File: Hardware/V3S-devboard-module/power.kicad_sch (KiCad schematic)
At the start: 19 parts, among them U2 EA3036C

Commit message: schematic improvements
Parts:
- added C14, C15: 106, symbol Device:C_Small
- added C16, C17, C20, C23, C25, C26, C29, C30, C33, C34, C35, C36, C37, C38, C39, C43: 100n, symbol Device:C_Small
- added C18, C21, C27, C31, C42: 10u, symbol Device:C_Small
- added C19, C22, C24, C28, C32, C40: 1u, symbol Device:C_Small
- added C41, C44: 4.7u, symbol Device:C_Small
- added R1: 0, symbol Device:R_Small_US
- added R12, R13: 2K, symbol Device:R_Small_US
- added R14: 200K, symbol Device:R_Small_US
- added U3: XC6206PxxxMR, Package_TO_SOT_SMD:SOT-23-3, symbol Regulator_Linear:XC6206PxxxMR
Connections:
- net 1V2: now also C21.2, C24.2, C25.2, C26.2, C27.2, C28.2, C29.2, C30.2
- net 1V8: now also C18.2, C19.2, C20.2, C22.2, C23.2, R12.1
- net 3V3: now also C31.2, C32.2, C33.2, C34.2, C35.2, C36.2, C39.2, R1.2, U3.3 (VI)
- net GND: now also C14.1, C15.1, C16.1, C17.1, C18.1, C19.1, C20.1, C21.1, C22.1, C23.1, C24.1, C25.1, C26.1, C27.1, C28.1, C29.1, C30.1, C31.1, C32.1, C33.1, C34.1, C35.1, C36.1, C37.1, C38.1, C39.1, C40.1, C41.1, C42.1, C43.1, C44.1, R13.2, R14.2, U3.1 (GND)
- net SVREF: now also C16.2, C17.2, R12.2, R13.1
- net VCC_HP_BP: now also C42.2, C43.2
- net VCC_RTC: now also C37.2, R1.1
- net VCC_RTCIO: now also C44.2
- net VRA1: now also C40.2
- net VRA2: now also C41.2, R14.1
- new net 3V0: C14.2, C15.2, C38.2, U3.2 (VO)

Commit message: general improvements. power almost complete
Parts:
- added C46: 10u, Capacitor_SMD:C_0805_2012Metric, symbol Device:C_Small
- C1, C14, C15: value 106 -> 1u; footprint (none) -> Capacitor_SMD:C_0805_2012Metric
- C16, C17, C20, C23, C25, C26, C29, C30, C33, C34, C35, C36, C37, C38, C39, C4, C43, C5, C6: footprint (none) -> Capacitor_SMD:C_0603_1608Metric
- C18, C19, C21, C22, C24, C27, C28, C31, C32, C40, C41, C42, C44: footprint (none) -> Capacitor_SMD:C_0805_2012Metric
- C2, C3, C7, C8, C9: value 106 -> 10u; footprint (none) -> Capacitor_SMD:C_0805_2012Metric
- L1, L2, L3: footprint (none) -> Inductor_SMD:L_1008_2520Metric
- R12, R13, R14, R2, R3, R4, R5, R6, R7: footprint (none) -> Resistor_SMD:R_0603_1608Metric
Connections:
- net 3V0: no longer C15.2
- net 3V3: now also C15.2
- net 5V: now also C46.1
- net GND: now also C46.2
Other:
- note added: "1uF near VCC 10uF near VINx"
- note added: "DC resistance must be < 100 milliohms Current rating 1.1A"
- moved on the sheet: C1, C2, C3

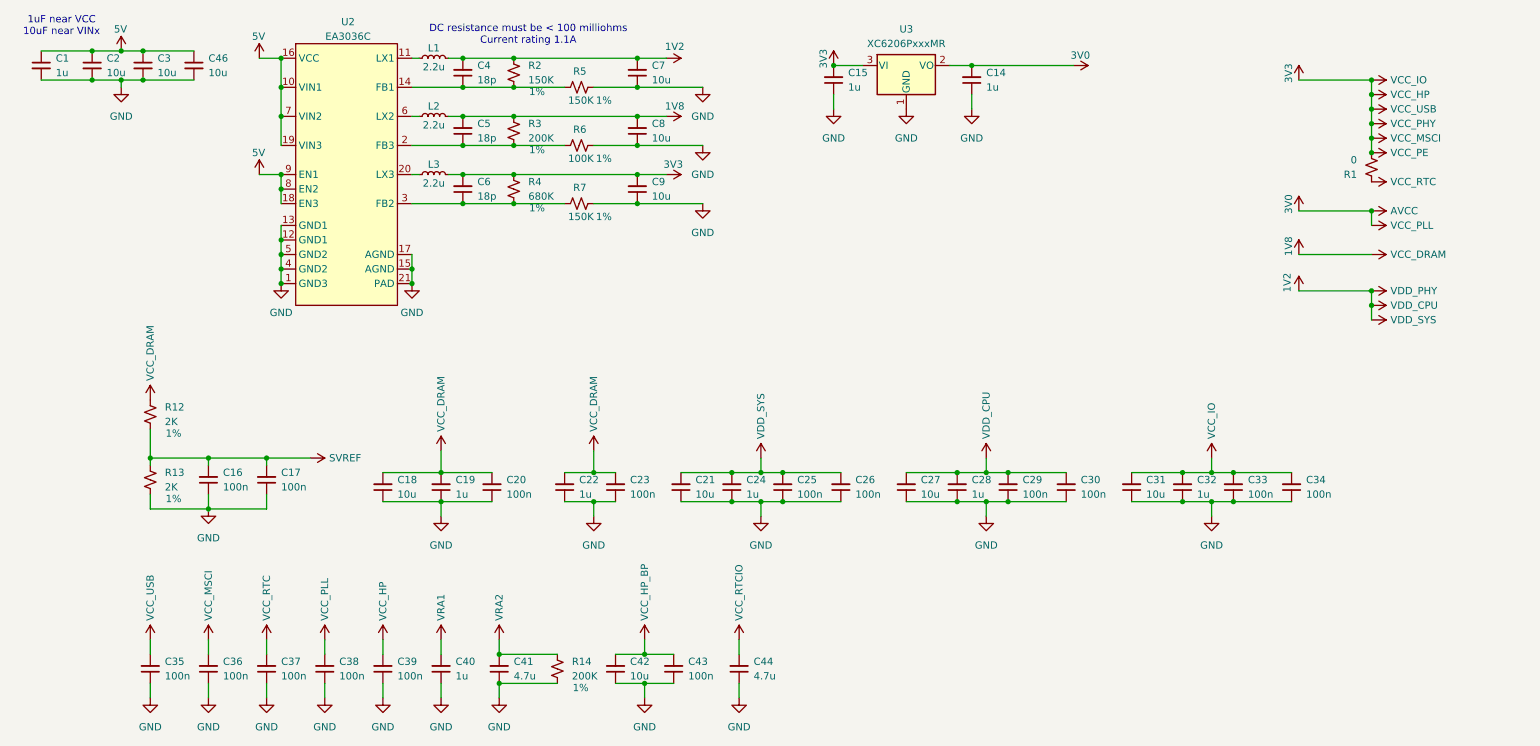
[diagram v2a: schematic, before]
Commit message: new power designators
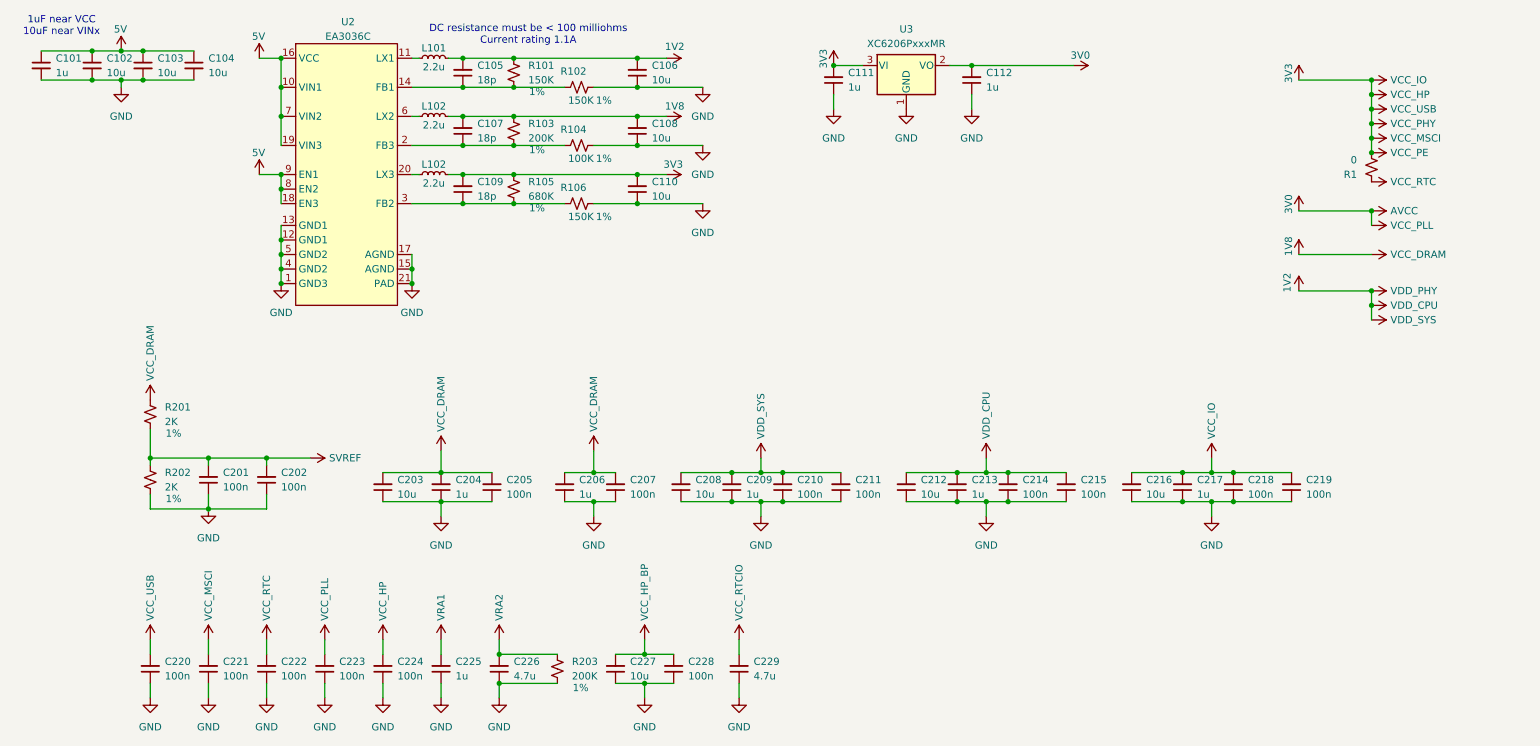
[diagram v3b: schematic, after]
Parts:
- renumbered C1 to C101, C2 to C102, C3 to C103, C46 to C104, C4 to C105, C7 to C106, C5 to C107, C8 to C108, C6 to C109, C9 to C110, C15 to C111, C14 to C112, C16 to C201, C17 to C202, C18 to C203, C19 to C204, C20 to C205, C22 to C206, C23 to C207, C21 to C208, C24 to C209, C25 to C210, C26 to C211, C27 to C212, C28 to C213, C29 to C214, C30 to C215, C31 to C216, C32 to C217, C33 to C218, C34 to C219, C35 to C220, C36 to C221, C37 to C222, C38 to C223, C39 to C224, C40 to C225, C41 to C226, C42 to C227, C43 to C228, C44 to C229, L1 to L101, L2 to L102, L3 to L102, R2 to R101, R5 to R102, R3 to R103, R6 to R104, R4 to R105, R7 to R106, R12 to R201, R13 to R202, R14 to R203

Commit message: minor improvements and fixes
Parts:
- R106: renamed from R1; footprint (none) -> Resistor_SMD:R_0603_1608Metric
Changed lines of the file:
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@@
 		(on_board yes)
 		(dnp no)
-		(property "Reference" "R1"
+		(property "Reference" "R106"
 			(at 255.27 58.4201 0)
 			(effects
@@
 			)
 		)
-		(property "Footprint" ""
+		(property "Footprint" "Resistor_SMD:R_0603_1608Metric"
 			(at 257.81 57.15 0)
 			(effects
@@
 			(project "V3S-devboard-module"
 				(path "/5d41c08e-2331-42df-a2d5-1aeb6ed4388c/5949d9b7-76b3-40a2-8931-5cd58c7934ef"
-					(reference "R1")
+					(reference "R106")
 					(unit 1)
 				)

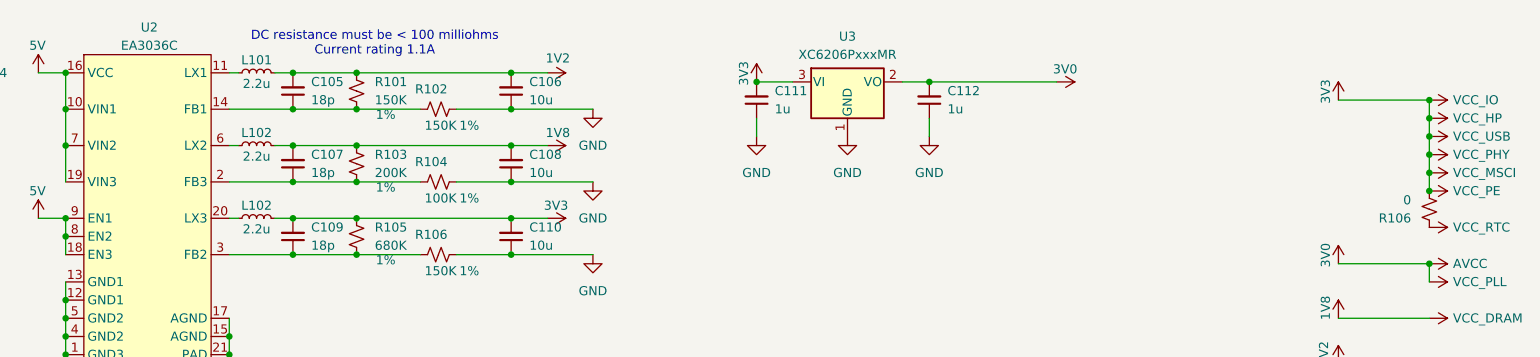
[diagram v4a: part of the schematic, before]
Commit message: fixed minor schematic issues
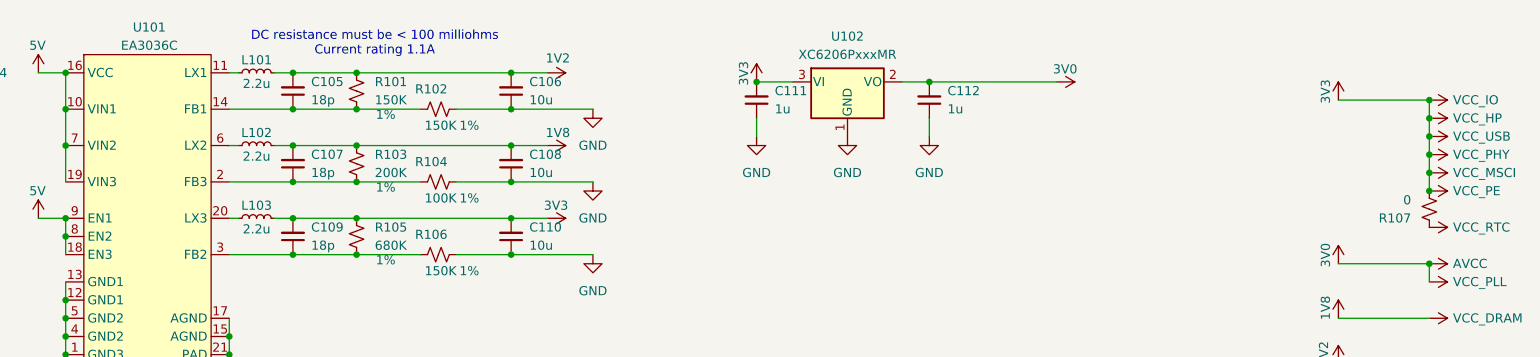
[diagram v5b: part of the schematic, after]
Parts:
- renumbered L102 to L103, R106 to R107, U2 to U101, U3 to U102
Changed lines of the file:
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@@
 		(dnp no)
 		(fields_autoplaced yes)
-		(property "Reference" "U3"
+		(property "Reference" "U102"
 			(at 176.53 33.02 0)
 			(effects
@@
 			(project "V3S-devboard-module"
 				(path "/5d41c08e-2331-42df-a2d5-1aeb6ed4388c/5949d9b7-76b3-40a2-8931-5cd58c7934ef"
-					(reference "U3")
+					(reference "U102")
 					(unit 1)
 				)
@@
 		(on_board yes)
 		(dnp no)
-		(property "Reference" "L102"
+		(property "Reference" "L103"
 			(at 93.98 56.642 90)
 			(effects
@@
 			(project "V3S-devboard-module"
 				(path "/5d41c08e-2331-42df-a2d5-1aeb6ed4388c/5949d9b7-76b3-40a2-8931-5cd58c7934ef"
-					(reference "L102")
+					(reference "L103")
 					(unit 1)
 				)
@@
 		(on_board yes)
 		(dnp no)
-		(property "Reference" "R106"
+		(property "Reference" "R107"
 			(at 255.27 58.4201 0)
 			(effects
@@
 			(project "V3S-devboard-module"
 				(path "/5d41c08e-2331-42df-a2d5-1aeb6ed4388c/5949d9b7-76b3-40a2-8931-5cd58c7934ef"
-					(reference "R106")
+					(reference "R107")
 					(unit 1)
 				)
@@
 		(on_board yes)
 		(dnp no)
-		(property "Reference" "U2"
+		(property "Reference" "U101"
 			(at 78.994 31.75 0)
 			(effects
@@
 			(project "V3S-devboard-module"
 				(path "/5d41c08e-2331-42df-a2d5-1aeb6ed4388c/5949d9b7-76b3-40a2-8931-5cd58c7934ef"
-					(reference "U2")
+					(reference "U101")
 					(unit 1)
 				)

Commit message: layout improvements.
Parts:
- added NT1: NetTie_2, NetTie:NetTie-2_SMD_Pad2.0mm, symbol Device:NetTie_2
- C101, C102, C103, C104, C106, C108, C110, C111, C112, C203, C204, C206, C208, C209, C212, C213, C216, C217, C225, C226, C227, C229: footprint Capacitor_SMD:C_0805_2012Metric -> Capacitor_SMD:C_0603_1608Metric
- C105, C107, C109, C202, C205, C207, C210, C211, C214, C215, C218, C219, C220, C221, C222, C223, C224, C228: footprint Capacitor_SMD:C_0603_1608Metric -> Capacitor_SMD:C_0402_1005Metric
- R101, R102, R103, R104, R105, R106, R201, R202, R203: footprint Resistor_SMD:R_0603_1608Metric -> Resistor_SMD:R_0402_1005Metric
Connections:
- net 1V8: now also NT1.1; no longer C203.2, C204.2, C205.2, C206.2, C207.2, R201.1
- new net VCC_DRAM: C203.2, C204.2, C205.2, C206.2, C207.2, NT1.2, R201.1
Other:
- moved on the sheet: C206, C207

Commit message: some layout
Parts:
- removed NT1: NetTie_2, NetTie:NetTie-2_SMD_Pad2.0mm, symbol Device:NetTie_2
- added NT10, NT11, NT12, NT13, NT2, NT3, NT4, NT5, NT6, NT7, NT8, NT9: NetTie_2, NetTie:NetTie-2_SMD_Pad0.5mm, symbol Device:NetTie_2
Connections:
- net 1V2: now also NT10.1, NT12.1, NT13.1; no longer C208.2, C209.2, C210.2, C211.2, C212.2, C213.2, C214.2, C215.2
- net 1V8: now also NT11.1
- net 3V0: now also NT8.1, NT9.1; no longer C223.2
- net 3V3: now also NT2.1, NT3.1, NT4.1, NT5.1, NT6.1, NT7.1; no longer C216.2, C217.2, C218.2, C219.2, C220.2, C221.2, C224.2
- net VCC_DRAM: now also NT11.2
- net at L101.1: now also U101.6 (LX2); no longer U101.11 (LX1)
- net at L102.1: now also U101.11 (LX1); no longer U101.6 (LX2)
- net at C107.1, R103.2, R104.1: now also U101.14 (FB1); no longer U101.2 (FB3)
- net at C105.1, R101.2, R102.1: now also U101.2 (FB3); no longer U101.14 (FB1)
- new net AVCC: NT8.2
- new net VCC_HP: C224.2, NT3.2
- new net VCC_IO: C216.2, C217.2, C218.2, C219.2, NT2.2
- new net VCC_MSCI: C221.2, NT6.2
- new net VCC_PE: NT7.2
- new net VCC_PHY: NT5.2
- new net VCC_PLL: C223.2, NT9.2
- new net VCC_USB: C220.2, NT4.2
- new net VDD_CPU: C212.2, C213.2, C214.2, C215.2, NT13.2
- new net VDD_PHY: NT12.2
- new net VDD_SYS: C208.2, C209.2, C210.2, C211.2, NT10.2
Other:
- moved on the sheet: C105, C106, C107, C108, L101, L102, R101, R102, R103, R104

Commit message: more layout
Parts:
- C201: footprint Capacitor_SMD:C_0603_1608Metric -> Capacitor_SMD:C_0402_1005Metric
- R107: footprint Resistor_SMD:R_0603_1608Metric -> Resistor_SMD:R_0402_1005Metric
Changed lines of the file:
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@@
 			)
 		)
-		(property "Footprint" "Resistor_SMD:R_0603_1608Metric"
+		(property "Footprint" "Resistor_SMD:R_0402_1005Metric"
 			(at 257.81 57.15 0)
 			(effects
@@
 			)
 		)
-		(property "Footprint" "Capacitor_SMD:C_0603_1608Metric"
+		(property "Footprint" "Capacitor_SMD:C_0402_1005Metric"
 			(at 54.61 111.76 0)
 			(effects
